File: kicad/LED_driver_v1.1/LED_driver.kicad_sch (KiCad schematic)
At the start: 7 parts, among them J1 Conn_01x02_Pin, J2 Conn_01x03_Pin

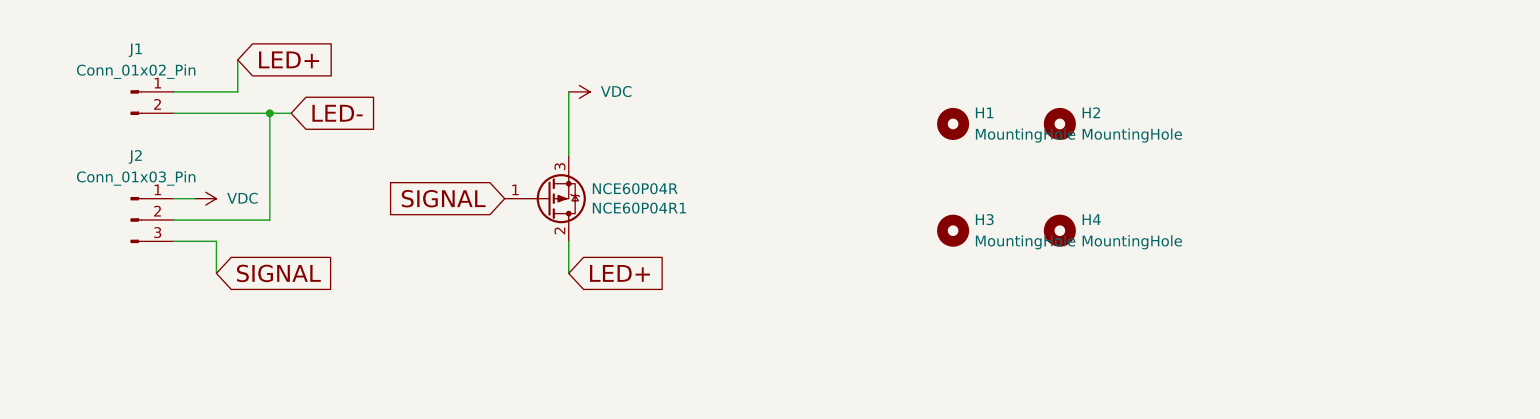
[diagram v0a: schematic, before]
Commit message: LED drive v2.0
redesigned the mos cus the old one probably doesn't work
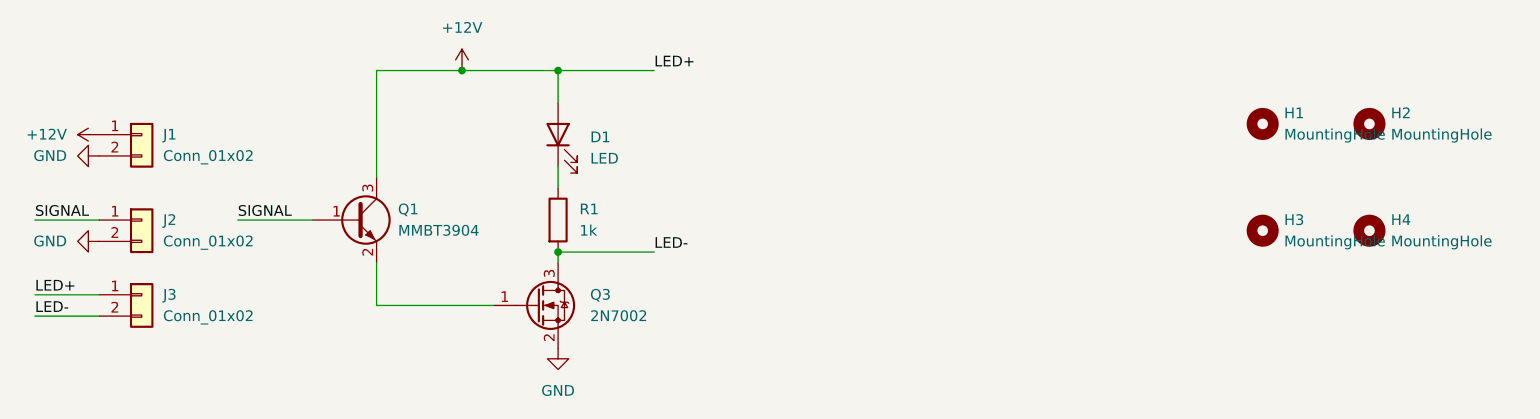
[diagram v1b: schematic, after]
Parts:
- removed J1: Conn_01x02_Pin, Connector_JST:JST_VH_B2P-VH_1x02_P3.96mm_Vertical, symbol Connector:Conn_01x02_Pin
- removed J2: Conn_01x03_Pin, Connector_JST:JST_VH_B3P-VH_1x03_P3.96mm_Vertical, symbol Connector:Conn_01x03_Pin
- removed NCE60P04R1: NCE60P04R, Package_TO_SOT_SMD:SOT-223-3_TabPin2, symbol Device:Q_PMOS_GDS
- added D1: LED, LED_SMD:LED_0805_2012Metric_Pad1.15x1.40mm_HandSolder, symbol Device:LED
- added J1, J2, J3: Conn_01x02, Connector_JST:JST_VH_B2P-VH_1x02_P3.96mm_Vertical, symbol Connector_Generic:Conn_01x02
- added Q1: MMBT3904, Package_TO_SOT_SMD:SOT-23_Handsoldering, symbol Transistor_BJT:MMBT3904
- added Q3: 2N7002, Package_TO_SOT_SMD:SOT-23_Handsoldering, symbol Transistor_FET:2N7002
- added R1: 1k, Resistor_SMD:R_0805_2012Metric_Pad1.20x1.40mm_HandSolder, symbol Device:R
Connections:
- net LED-: now also J3.2 (Pin_2), Q3.3 (D), R1.2
- net SIGNAL: now also J2.1 (Pin_1), Q1.1 (B)
- new net: D1.1 (K), R1.1
- new net: Q1.2 (E), Q3.1 (G)
- new net +12V: D1.2 (A), J1.1 (Pin_1), J3.1 (Pin_1), Q1.3 (C)
- new net GND: J1.2 (Pin_2), J2.2 (Pin_2), Q3.2 (S)
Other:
- moved on the sheet: H1, H2, H3, H4
